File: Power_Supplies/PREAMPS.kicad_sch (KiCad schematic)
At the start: 142 parts, among them J14 AudioJack2, J15 XLR3_AudioJack3_Combo, J16 AudioJack2, J17 AudioJack2, J18 AudioJack2, J19 XLR3_AudioJack3_Combo, J20 XLR3_AudioJack3_Combo, J21 XLR3_AudioJack3_Combo, SW3 SW_Push, SW7 SW_Push, SW8 SW_Push, SW9 SW_Push, U25 OPA2134, U26 SSM2019BRNZ, U27 OPA2134, U28 SSM2019BRNZ, U29 SSM2019BRNZ, U30 SSM2019BRNZ

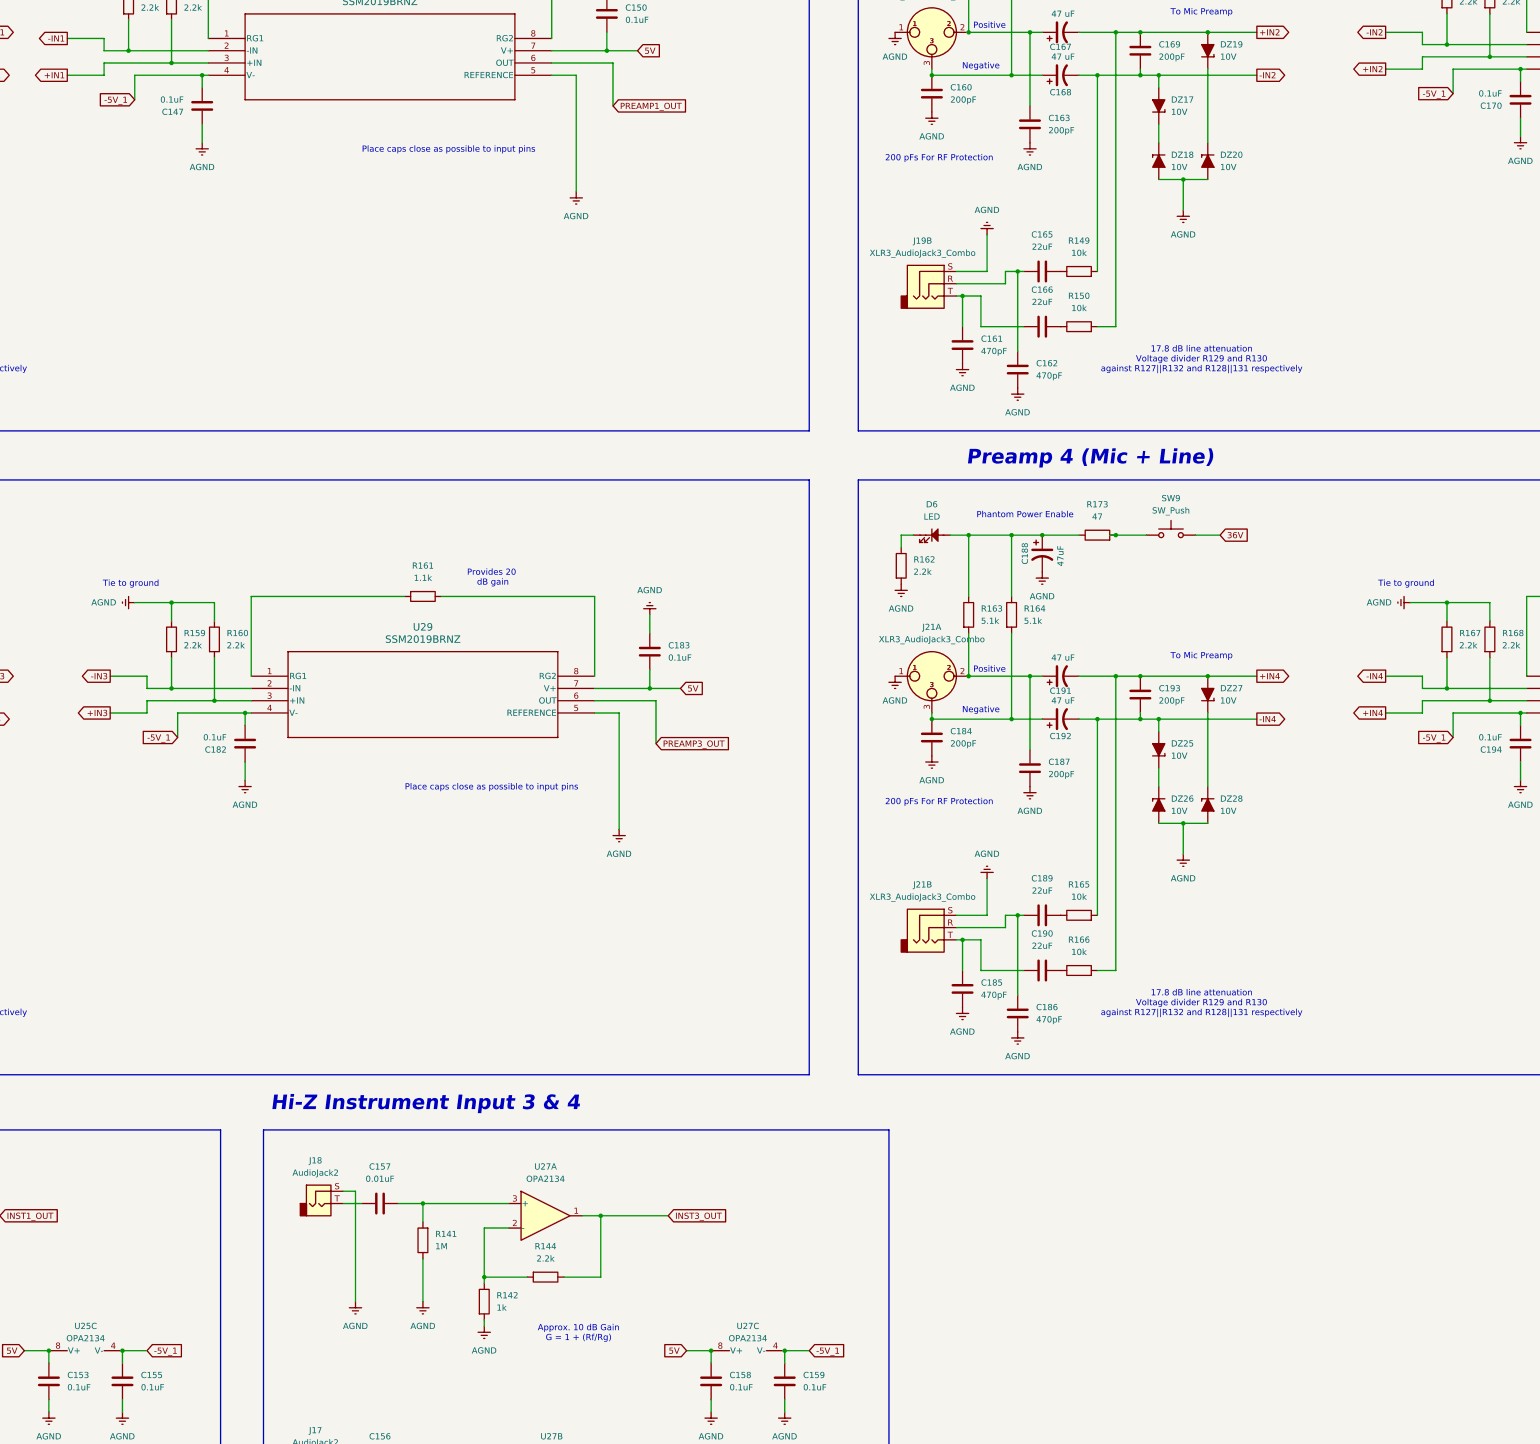
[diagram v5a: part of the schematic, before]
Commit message: Added 3.3V/1.8V LDO, clock IC
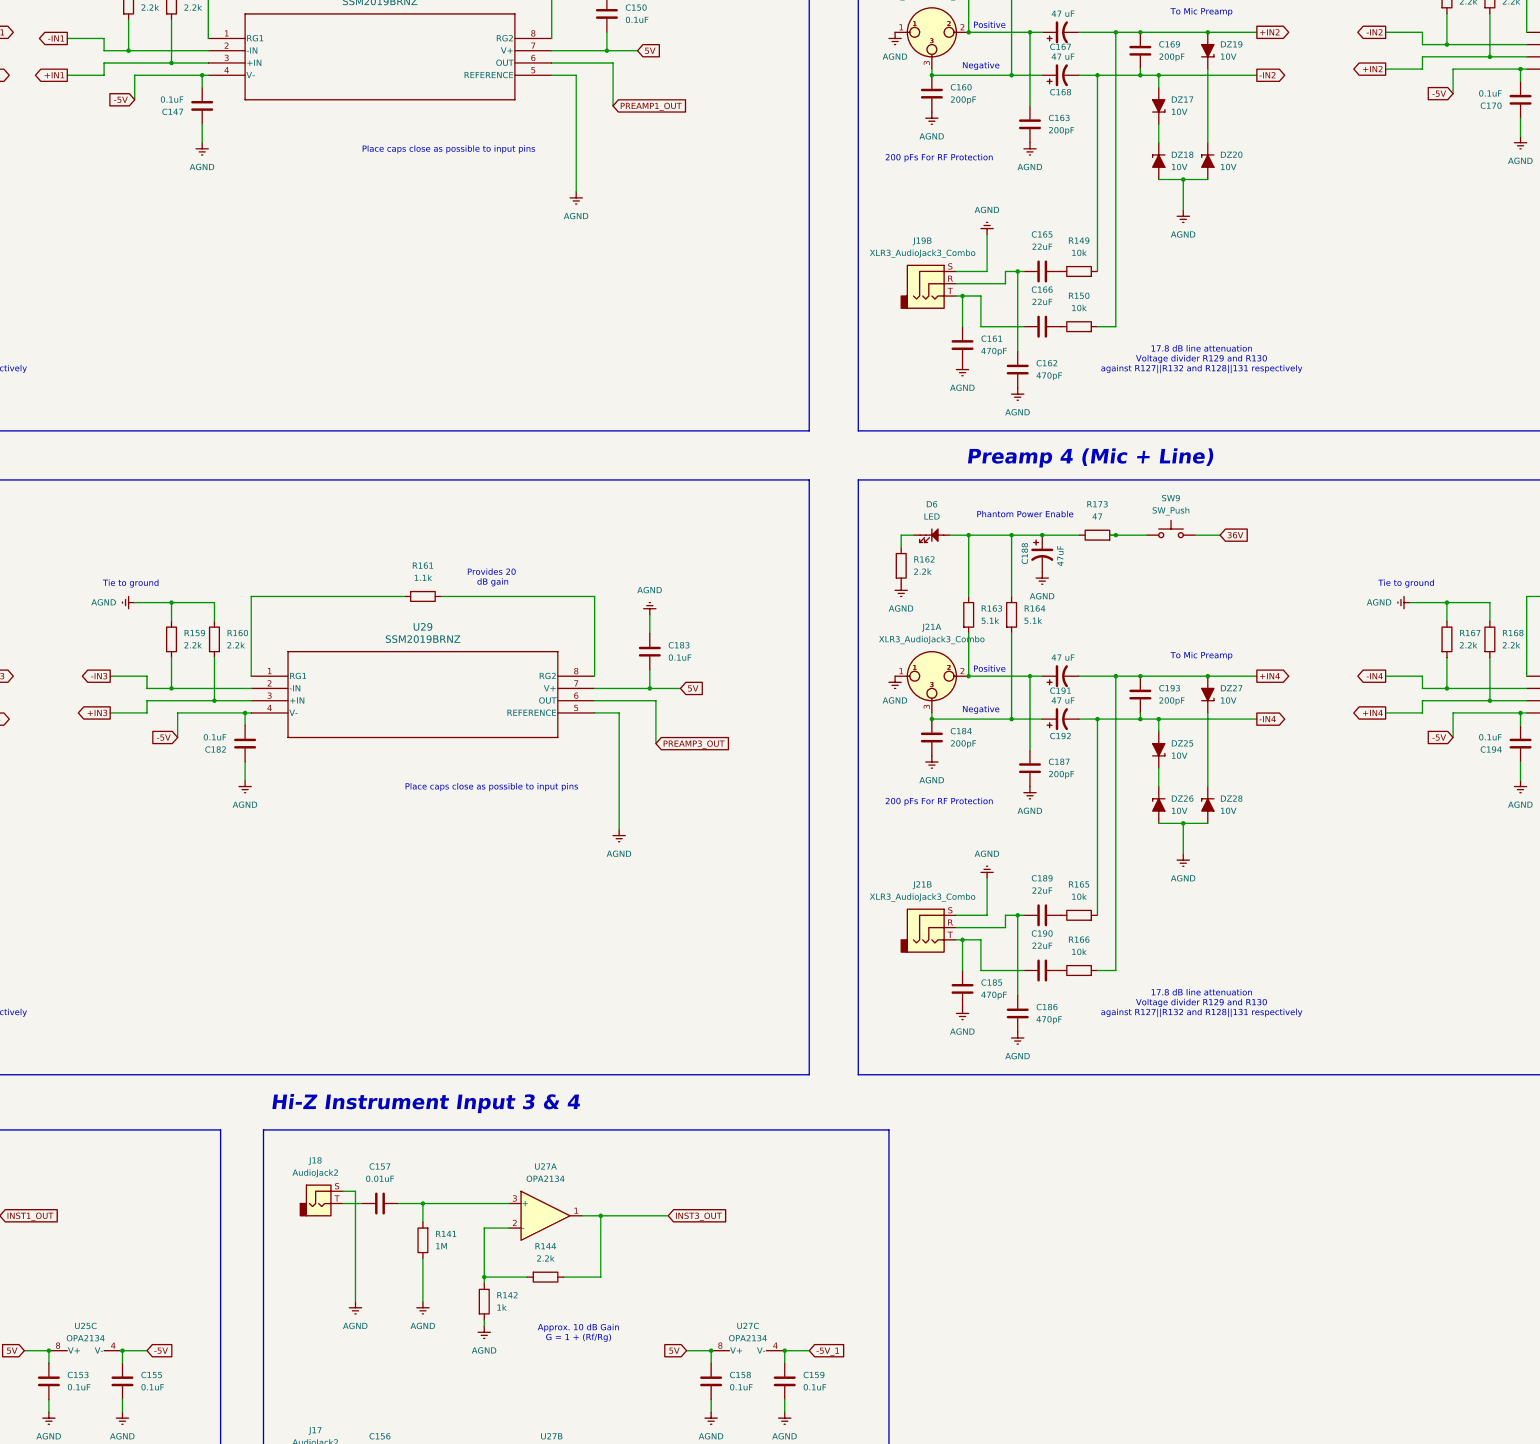
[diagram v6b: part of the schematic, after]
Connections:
- net -5V_1: no longer C147.1, C155.2, C170.1, C182.1, C194.1, U25.4 (V-), U26.4 (V-), U28.4 (V-), U29.4 (V-), U30.4 (V-)
- new net -5V: C147.1, C155.2, C170.1, C182.1, C194.1, U25.4 (V-), U26.4 (V-), U28.4 (V-), U29.4 (V-), U30.4 (V-)

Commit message: big things are coming...
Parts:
- removed J14, J16, J17, J18: AudioJack2, symbol Connector_Audio:AudioJack2
- added J20, J5, J6, J7: ACJM-MV-2, ACJMMV2, symbol SamacSys_Parts:ACJM-MV-2
- J10: renamed from J21; footprint (none) -> Connector_Audio:Jack_XLR-6.35mm_Neutrik_NCJ5FI-H-0_Horizontal
- J3: renamed from J15; footprint (none) -> Connector_Audio:Jack_XLR-6.35mm_Neutrik_NCJ5FI-H-0_Horizontal
- J4: renamed from J20; footprint (none) -> Connector_Audio:Jack_XLR-6.35mm_Neutrik_NCJ5FI-H-0_Horizontal
- J9: renamed from J19; footprint (none) -> Connector_Audio:Jack_XLR-6.35mm_Neutrik_NCJ5FI-H-0_Horizontal
- U15: renamed from U25; footprint (none) -> SamacSys_Parts:SOIC127P600X175-8N
- U18: renamed from U27; footprint (none) -> SamacSys_Parts:SOIC127P600X175-8N
- renumbered C167 to C100, C168 to C101, C191 to C102, C192 to C103, C169 to C104, C193 to C105, C170 to C106, C194 to C107, C171 to C108, C195 to C109, C140 to C54, C172 to C55, C149 to C56, C173 to C57, C152 to C58, C154 to C59, C151 to C60, C174 to C61, C142 to C62, C175 to C63, C143 to C64, C148 to C65, C141 to C66, C176 to C67, C177 to C68, C178 to C69, C144 to C70, C145 to C71, C179 to C72, C180 to C73, C146 to C74, C181 to C75, C153 to C76, C155 to C77, C147 to C78, C182 to C79, C157 to C80, C156 to C81, C150 to C82, C183 to C83, C158 to C84, C159 to C85, C160 to C86, C184 to C87, C161 to C88, C185 to C89, C162 to C90, C186 to C91, C163 to C92, C187 to C93, C164 to C94, C165 to C95, C166 to C96, C188 to C97, C189 to C98, C190 to C99, D3 to D1, D5 to D2, D4 to D3, D6 to D4, DZ13 to DZ1, DZ18 to DZ10, DZ25 to DZ11, DZ26 to DZ12, DZ19 to DZ13, DZ20 to DZ14, DZ27 to DZ15, DZ28 to DZ16, DZ14 to DZ2, DZ21 to DZ3, DZ22 to DZ4, DZ15 to DZ5, DZ16 to DZ6, DZ23 to DZ7, DZ24 to DZ8, DZ17 to DZ9, R126 to R42, R154 to R43, R127 to R44, R155 to R45, R128 to R46, R156 to R47, R133 to R48, R137 to R49, R130 to R50, R129 to R51, R157 to R52, R158 to R53, R172 to R54, R136 to R55, R170 to R56, R138 to R57, R134 to R58, R139 to R59, R131 to R60, R132 to R61, R159 to R62, R160 to R63, R135 to R64, R161 to R65, R141 to R66, R140 to R67, R142 to R68, R143 to R69, R144 to R70, R145 to R71, R146 to R72, R162 to R73, R147 to R74, R163 to R75, R148 to R76, R164 to R77, R149 to R78, R150 to R79, R165 to R80, R166 to R81, R171 to R82, R173 to R83, R151 to R84, R167 to R85, R152 to R86, R168 to R87, R153 to R88, R169 to R89, SW8 to SW1, SW3 to SW2, SW7 to SW3, SW9 to SW4, U26 to U16, U29 to U17, U28 to U19, U30 to U20
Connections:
- net AGND: now also J20.3, J5.3, J6.3, J7.3
- net at C80.2: now also J7.1
- net at C81.2: now also J6.1
- net at C59.2: now also J5.1
- net at C58.2: now also J20.1
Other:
- note added: "S"
- note added: "T"
- moved on the sheet: C80, C81

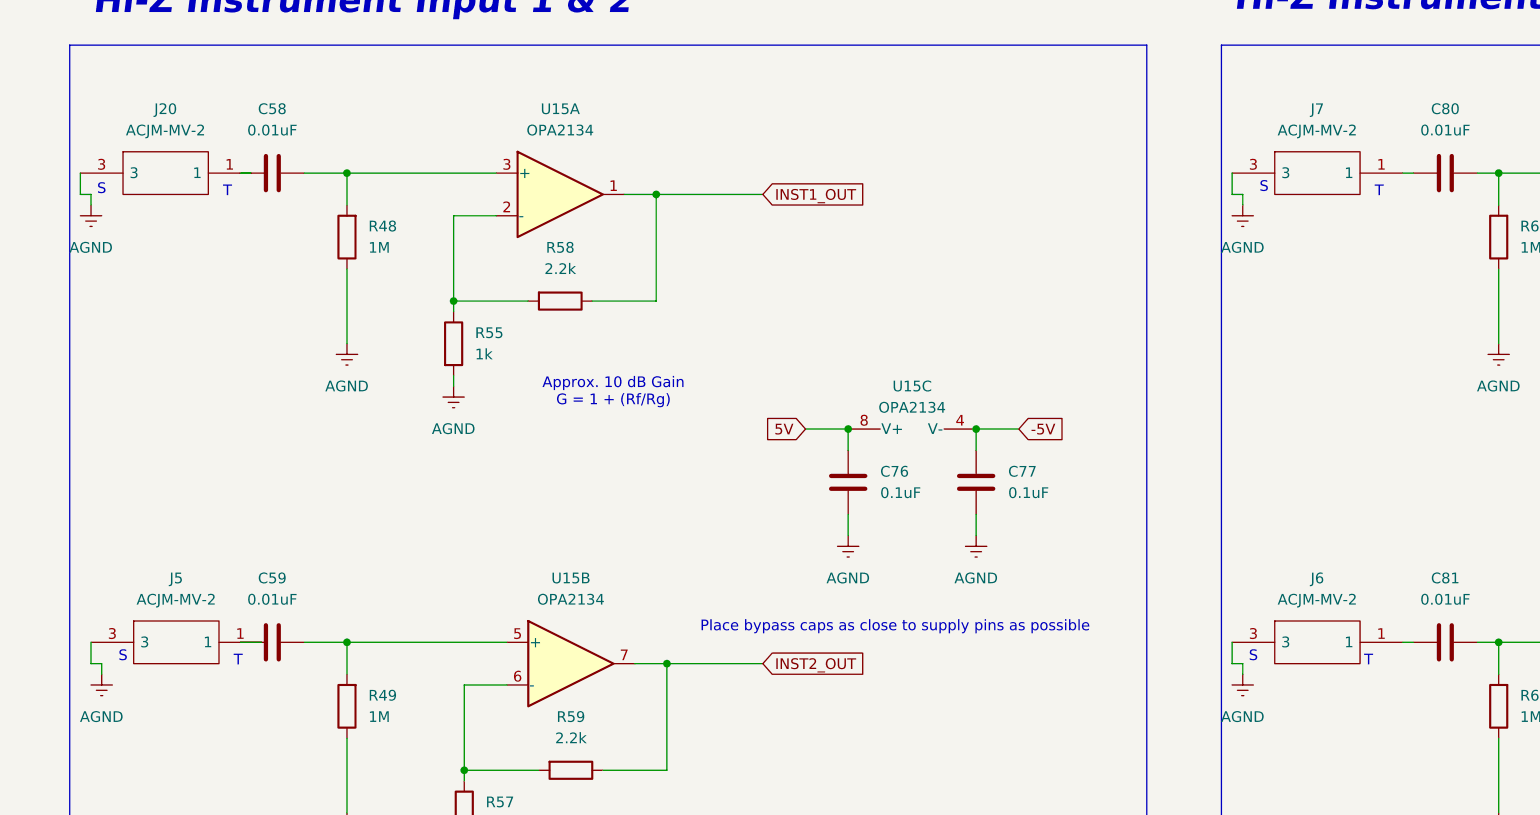
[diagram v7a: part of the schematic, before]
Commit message: added both ADCs, added differential output to DACs
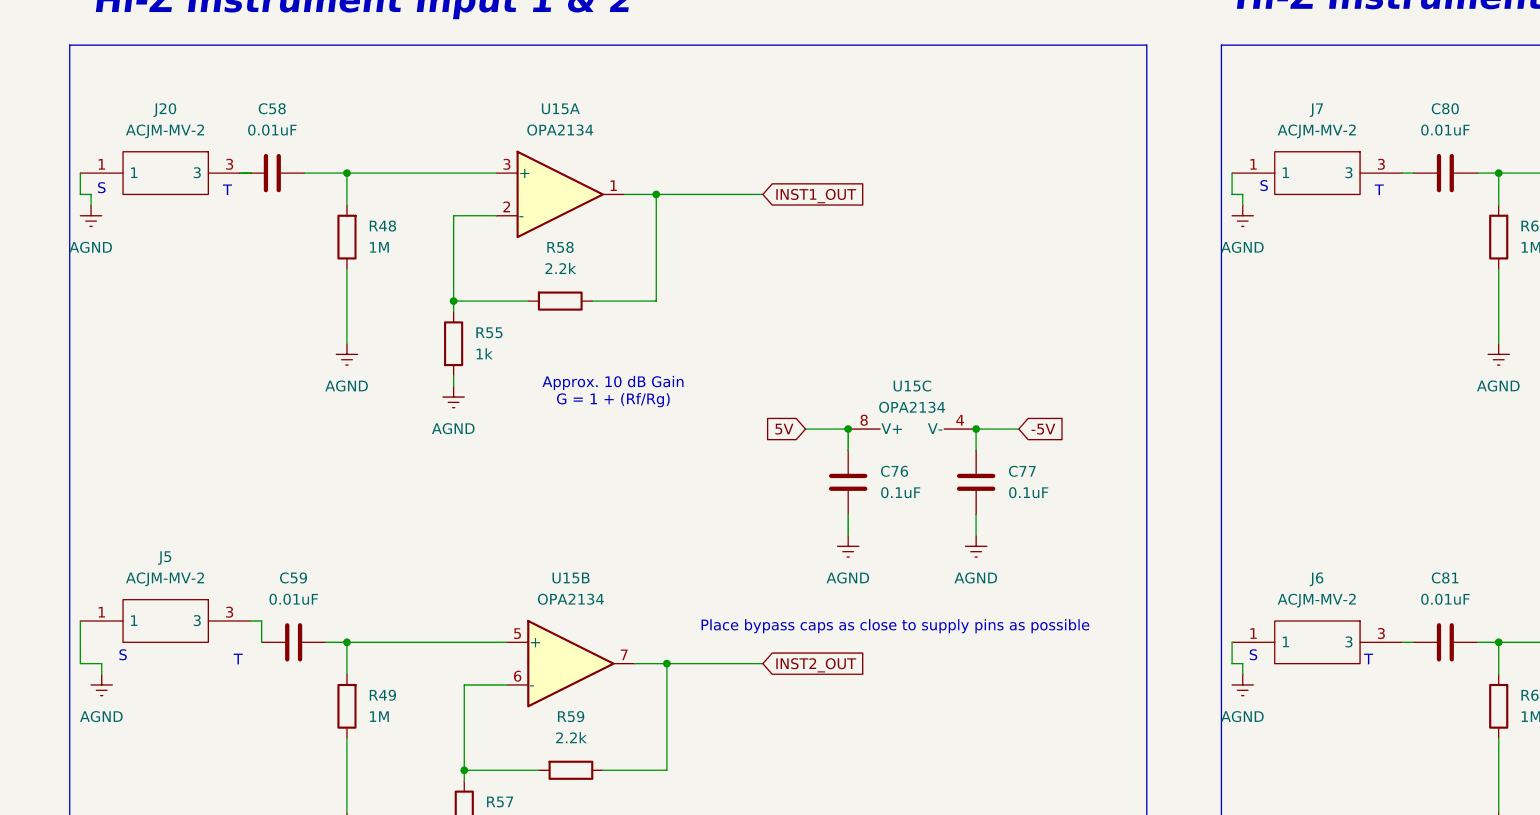
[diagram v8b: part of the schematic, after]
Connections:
- net AGND: now also J20.1, J5.1, J6.1, J7.1; no longer J20.3, J5.3, J6.3, J7.3
- net at C58.2: now also J20.3; no longer J20.1
- net at C59.2: now also J5.3; no longer J5.1
- net at C81.2: now also J6.3; no longer J6.1
- net at C80.2: now also J7.3; no longer J7.1
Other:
- moved on the sheet: C59
